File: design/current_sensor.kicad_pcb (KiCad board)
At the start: 2 copper layers, 58.5 x 25 mm, 40 parts, among them J1 DS conn, J2 DS conn, J3 Conn, J4 DS conn, T2 TRANS-2CT, U1 Buffer, U2 OPA376AID, U3 AMC1303, U4 Buffer, U5 SN6501DBV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

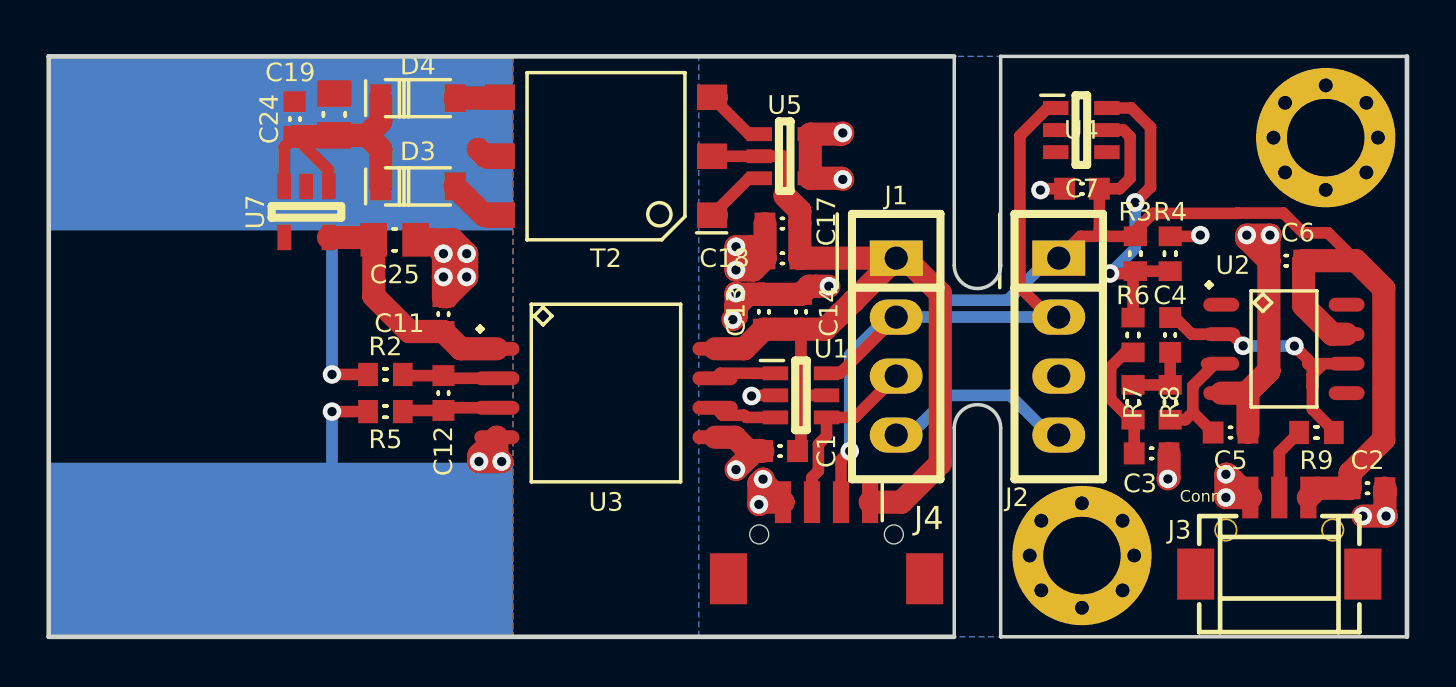
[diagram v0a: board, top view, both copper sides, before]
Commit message: Added buffer to restore signal before opamp analog filter
Signed-off-by: Marcos Chaparro <mchaparro@paltatech.com>
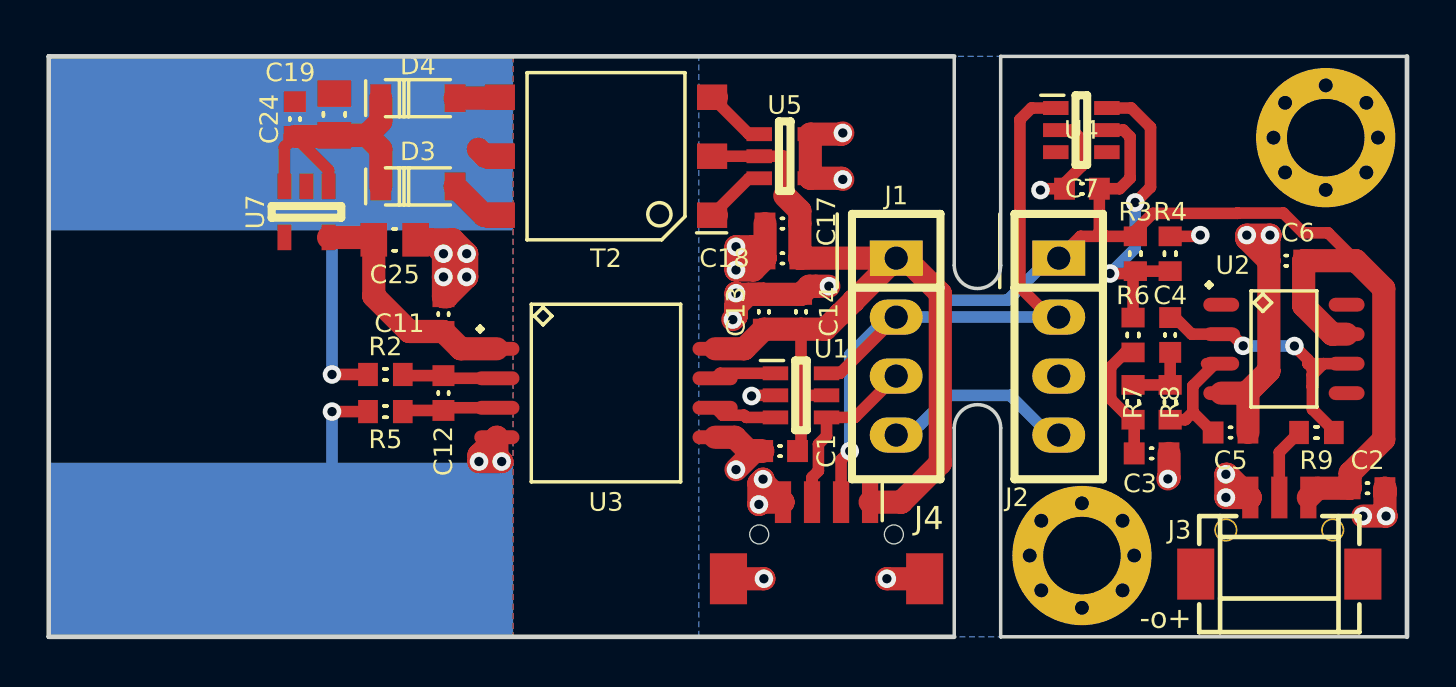
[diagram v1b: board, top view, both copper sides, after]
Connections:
- J4 pad : (no net) -> GND
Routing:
- net GND: track 58.5 -> 65.4 mm, vias 20 -> 22
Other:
- rule pad_to_mask_clearance: 0.2 -> 0.1
- board text added: "-o+"
- board text added: "CLK"
- board text added: "GND"
- board text added: "GND CLK ΔΣ VCC"
- board text added: "VCC"
- board text added: "ΔΣ"

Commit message: Added harness fault protections
Signed-off-by: Marcos Chaparro <mchaparro@paltatech.com>
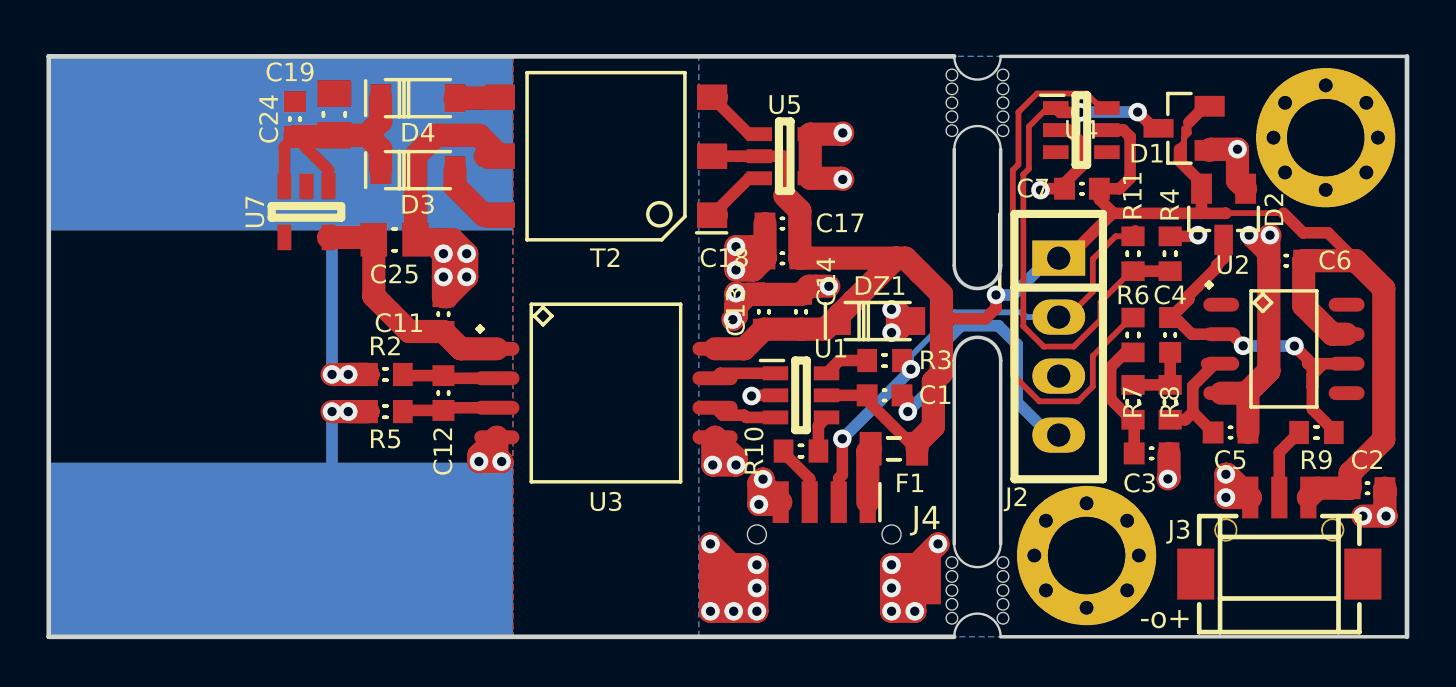
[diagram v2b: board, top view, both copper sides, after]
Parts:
- removed J1: DS conn, conn-100mil:CONN-100MIL-F-1x4
- added D1: BAT54S, smd-semi:SOT-23, F.Cu at (181.9, 75.1)
- added D2: BAT54S, smd-semi:SOT-23, F.Cu at (183.6, 78.8)
- added DZ1: MMSZ52XXB, smd-semi:SOD-123, F.Cu at (168.7, 83.4)
- added F1: FUSE 300mA, IPC7351-Nominal:RESC2012X50, F.Cu at (169.4, 88.9)
- added R10: 22R, IPC7351-Nominal:RESC1608X50, F.Cu at (165.4, 89.0)
- added R11: 220R, IPC7351-Nominal:RESC1608X50, F.Cu at (179.7, 80.5)
- added REF**: routing_tab_2mm_slot, routing_tab_2mm_slot, F.Cu at (173.0, 74.0)
- added REF**: routing_tab_2mm_slot, routing_tab_2mm_slot, F.Cu at (173.0, 95.0)
- R3: value 100k -> 22R
- U4: value Buffer -> SN74LVC2G17DBVR
- moved R3 11.7 mm to (169.0, 85.1), turned to 0 degrees
- moved C1 5.10 mm to (169.0, 86.6), turned to 0 degrees
- moved D3 0.70 mm to (148.9, 76.9)
- moved HOLE2 0.20 mm to (177.7, 93.5)
- moved J4 0.10 mm to (166.4, 94.5)
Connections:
- net /current sensor/VIN- renamed Net-(C12-Pad2)
- J4 pad 1: +5 -> Net-(F1-Pad1)
- R3 pad 1: +5 -> Net-(R3-Pad1)
- R3 pad 2: Net-(R3-Pad2) -> /delta_sigma
- R4 pad 1: Net-(R3-Pad2) -> Net-(D1-Pad3)
- R6 pad 2: Net-(R3-Pad2) -> Net-(R6-Pad2)
- U1 pad 4: /clk -> Net-(R10-Pad1)
- U1 pad 6: /delta_sigma -> Net-(R3-Pad1)
- U4 pad 1: /delta_sigma -> Net-(D1-Pad3)
- U4 pad 6: Net-(R3-Pad2) -> Net-(R6-Pad2)
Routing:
- net GND: track 65.4 -> 99.5 mm, vias 22 -> 36
- net Net-(R6-Pad2): track 0.00 -> 23.7 mm
- net Net-(D1-Pad3): track 0.00 -> 23.7 mm, vias 0 -> 2
- net Net-(R3-Pad2): track 14.0 -> 0.00 mm, vias 2 -> 0
- net /delta_sigma: track 31.4 -> 21.6 mm, vias 1 -> 2
- net ISOGND: track 23.0 -> 31.4 mm, vias 7 -> 8
- net /clk: track 7.65 -> 2.67 mm
- net Net-(C4-Pad1): track 14.2 -> 18.5 mm
- net Net-(F1-Pad1): track 0.00 -> 2.39 mm
- net Net-(R3-Pad1): track 0.00 -> 1.98 mm
- net Net-(R10-Pad1): track 0.00 -> 1.59 mm
- net /current sensor/Vin+: track 12.4 -> 13.3 mm, vias 1 -> 2
- net +5: track 91.4 -> 92.2 mm, vias 0 -> 1
- net Net-(D3-Pad2): track 2.44 -> 3.14 mm
- net Net-(C19-Pad1): track 12.5 -> 11.8 mm
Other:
- outline, holes or cut-outs redrawn
